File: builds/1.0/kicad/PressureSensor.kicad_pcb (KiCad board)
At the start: 2 copper layers, 38.1 x 57.2 mm, 22 parts, among them J1 PROG, U1 SENSOR, U2 HX710, U3 DISPLAY, U4 AVR64DD32

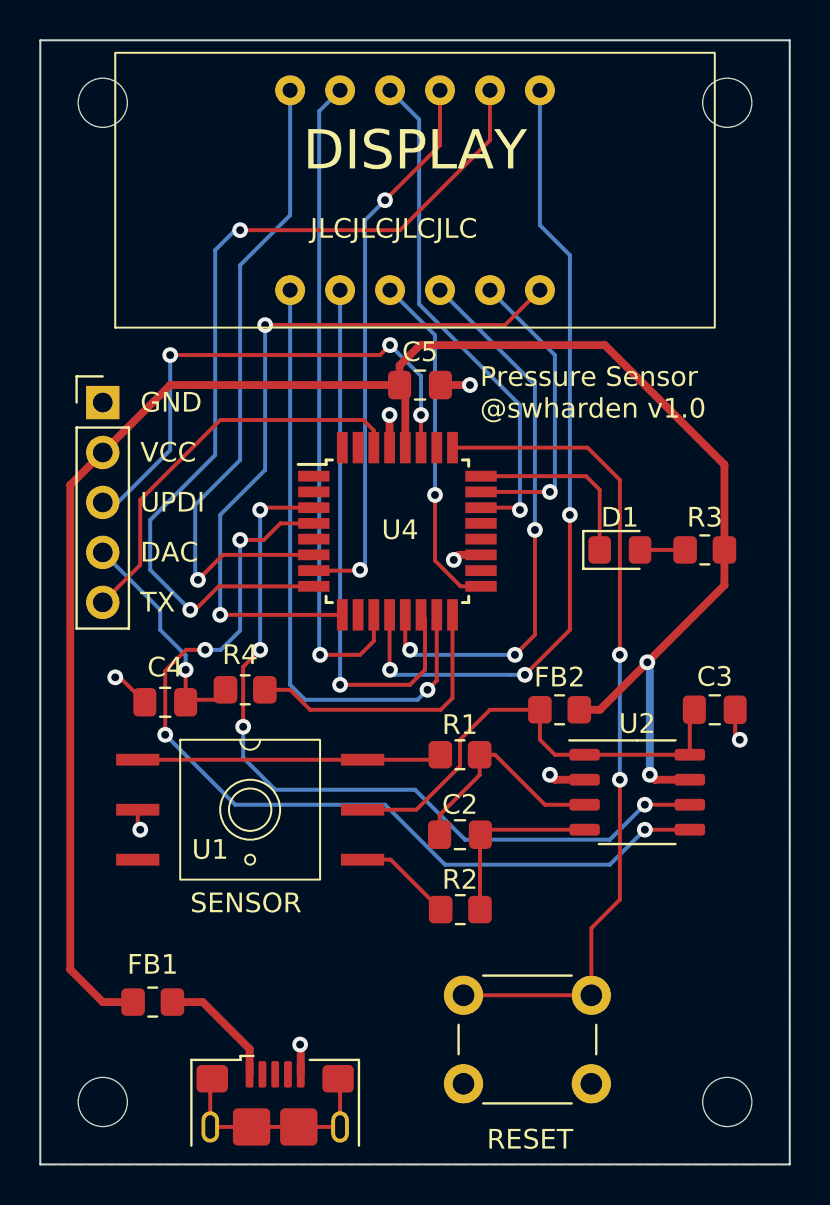
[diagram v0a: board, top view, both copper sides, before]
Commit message: update gerbers
move drill holes under display
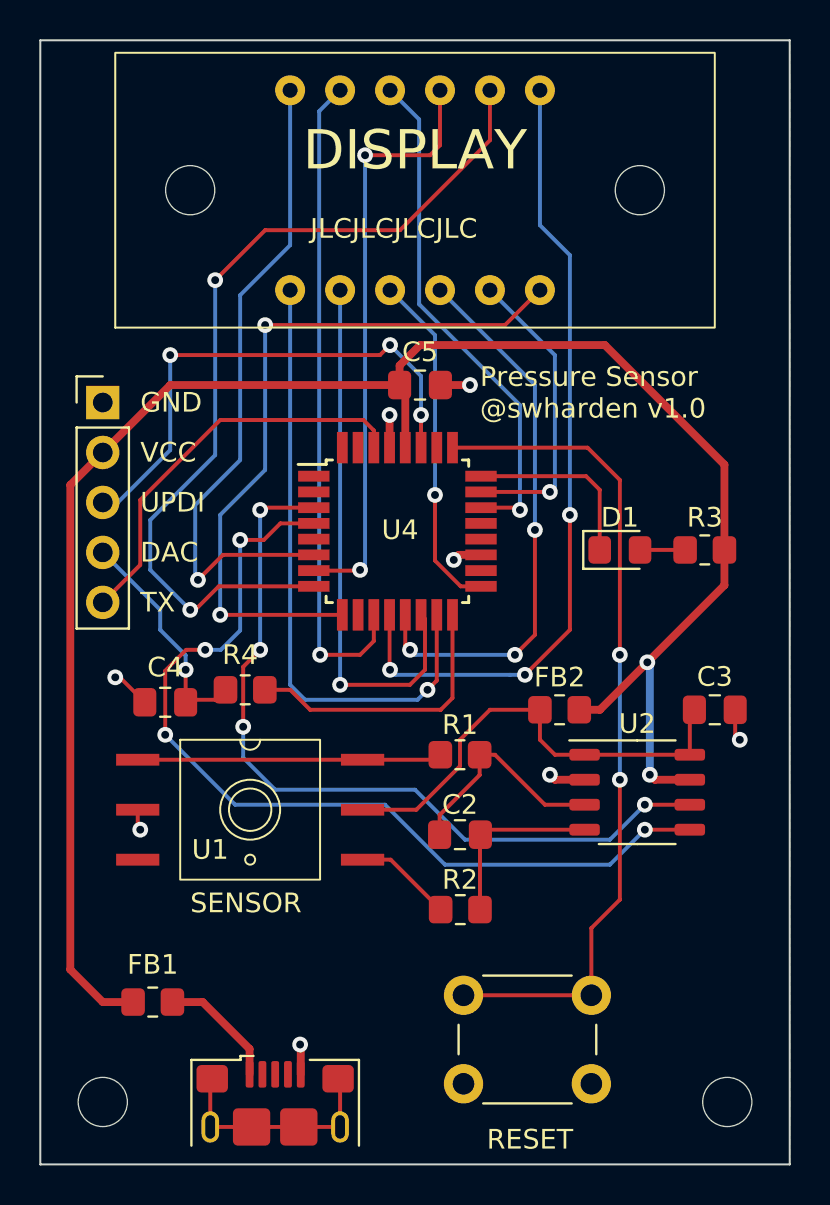
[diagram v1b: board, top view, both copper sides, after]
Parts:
- moved REF** 6.29 mm to (132.1, 58.4)
- moved REF** 6.29 mm to (109.2, 58.4)
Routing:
- net DIG_2: track 28.4 -> 30.4 mm
- net DIG_3: track 46.1 -> 45.2 mm
